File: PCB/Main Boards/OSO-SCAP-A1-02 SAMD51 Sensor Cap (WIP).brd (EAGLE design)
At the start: 50.8 x 22.9 mm, 70 parts, among them J1 10118193-0001LF, J2 S2B-PH-SM4-TB(LF)(SN), J3 S3B-PH-SM4-TB(LF)(SN), J4 SM04B-SRSS-TB(LF)(SN), Q1 DMG341, SW1 SPST_TACT-KMR2, SW2 SPST_TACT-KMR2, U1 AP2112-3.3, U2 MCP73831T-2ACI/OT, U3 ATSAMD51G18A-MUT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

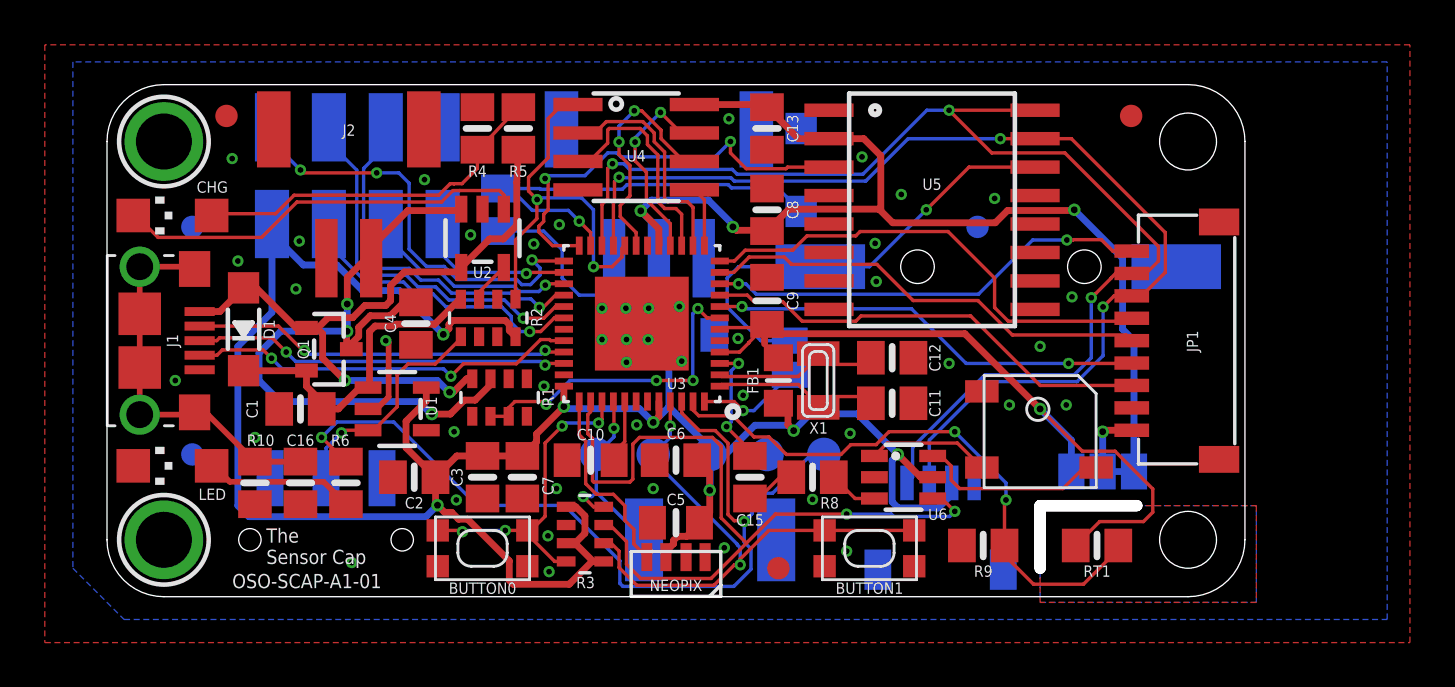
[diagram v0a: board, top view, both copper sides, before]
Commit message: A1 rev 02: add i2c pull-ups
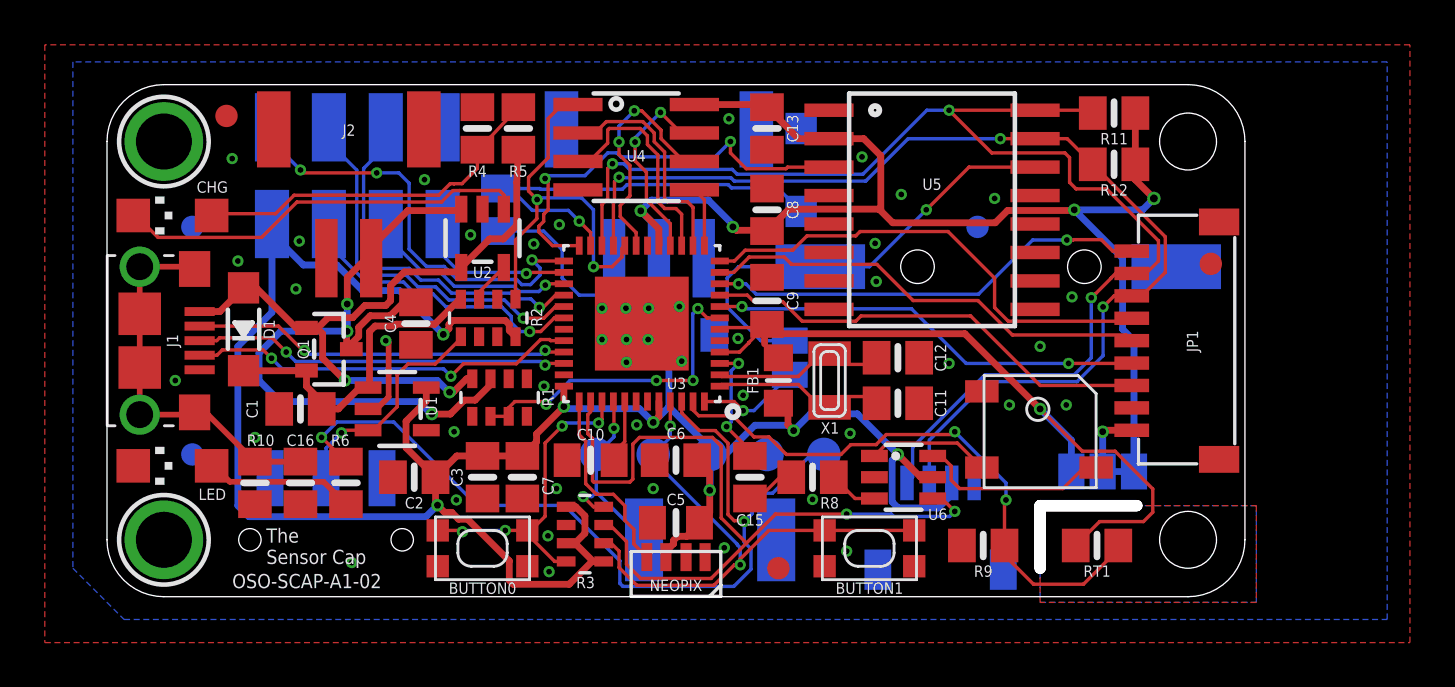
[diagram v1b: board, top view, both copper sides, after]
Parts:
- added R11, R12: 50K, microbuilder:0805-NO
- moved FID2 7.50 mm to (49.3, 14.9)
- moved X1 0.51 mm to (32.3, 9.65)
- moved C11 0.25 mm to (35.3, 8.64)
- moved C12 0.25 mm to (35.3, 10.7)
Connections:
- net +3V3: now also R11.2, R12.2
- net SCL: now also R11.1
- net SDA: now also R12.1
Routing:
- net +3V3: track 159.1 -> 167.0 mm, vias 10 -> 11
- net SCL: track 54.3 -> 57.7 mm
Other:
- board text added: "OSO-SCAP-A1-02"
- board text added: "The Sensor Cap Main Board OSO-SCAP-A1-02"
- board text removed: "OSO-SCAP-A1-01"
- board text removed: "The Sensor Cap Main Board OSO-SCAP-A1-01"

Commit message: CHG and FUL now separate LEDs
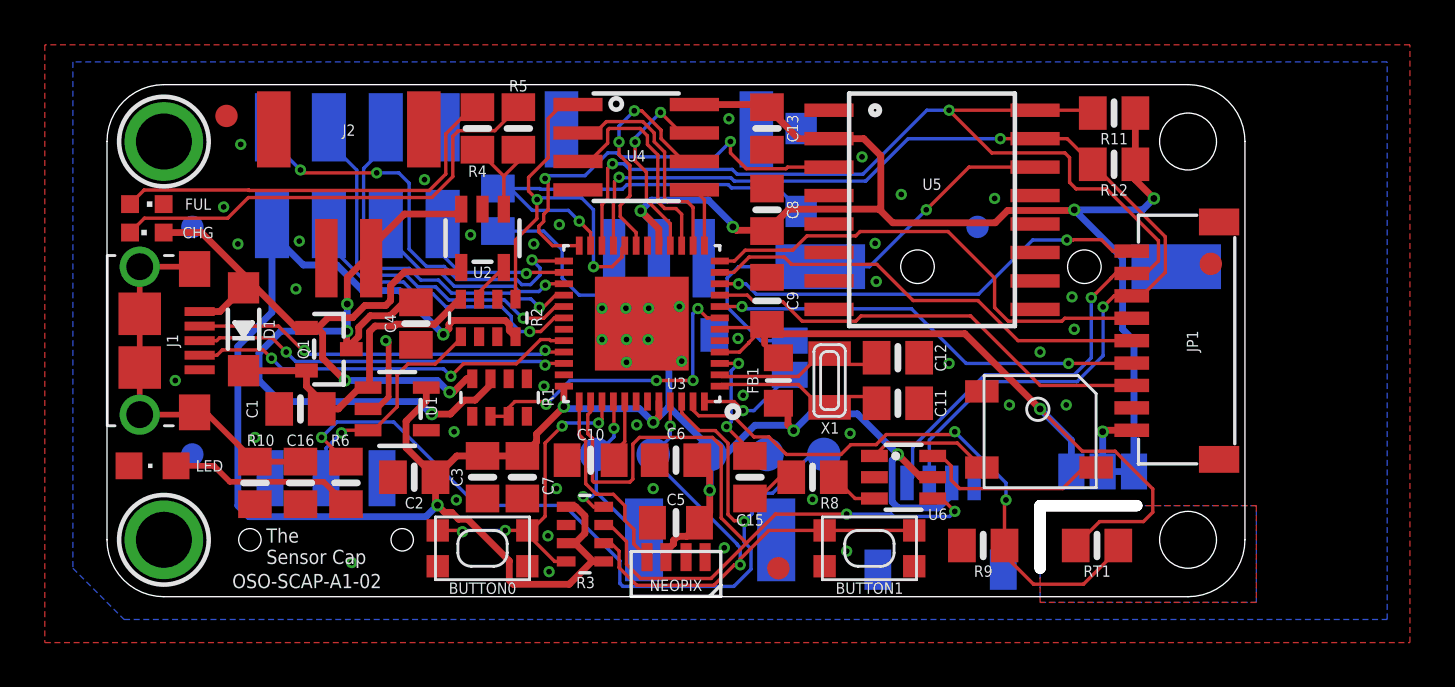
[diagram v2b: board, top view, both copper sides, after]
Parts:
- added FUL: GREEN, adafruit:CHIPLED_0603
- CHG: value YELLOW/GREEN -> AMBER; device My Stuff:CHIPLED_1206 -> adafruit:CHIPLED_0603
- LED: device adafruit:CHIPLED_1206 -> adafruit:CHIPLED_0805
- R4, R5: value 220~270 -> 1K
- moved CHG 1.37 mm to (1.78, 16.3)
- moved LED 0.89 mm to (2.03, 5.84)
- turned R5 to 90 degrees
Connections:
- removed net N$1: CHG.A, R4.2, R5.1
- new net N$6: CHG.C, R5.2
- new net N$7: FUL.A, R4.1
- net GND: now also FUL.C; no longer R4.1
- net STAT: now also R4.2, R5.1; no longer CHG.C
- net VBUS: now also CHG.A; no longer R5.2
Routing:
- net N$6: track 0.00 -> 20.7 mm
- net N$7: track 0.00 -> 18.4 mm
- net N$1: track 16.2 -> 0.00 mm
- net STAT: track 18.5 -> 4.59 mm
- net VBUS: track 30.5 -> 28.8 mm
- net N$2: track 6.71 -> 8.30 mm
- net GND: vias 46 -> 48
